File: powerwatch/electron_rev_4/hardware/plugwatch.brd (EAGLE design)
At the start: 57.1 x 93 mm, 124 parts, among them J1 DM3AT-SF-PEJM5, J2 TC2030-JLINK-NL, Q1 SI223DDS, U1 BGA725L6-ALT, U10 SIP32510, U11 SIP32510, U12 SIP32510, U13 SIP32510, U14 MPU-9250, U15 TPS3839G25DBZ, U2 SAFFB1G56KB0F0A, U3 ISL29035, U4 MAX-M8, U5 MAX740XESA, U6 SIP32510, U7 NRF51822QF, U8 OPA322AIDBVT, U9 SIP32510, X1 32.768k, X2 16MHz

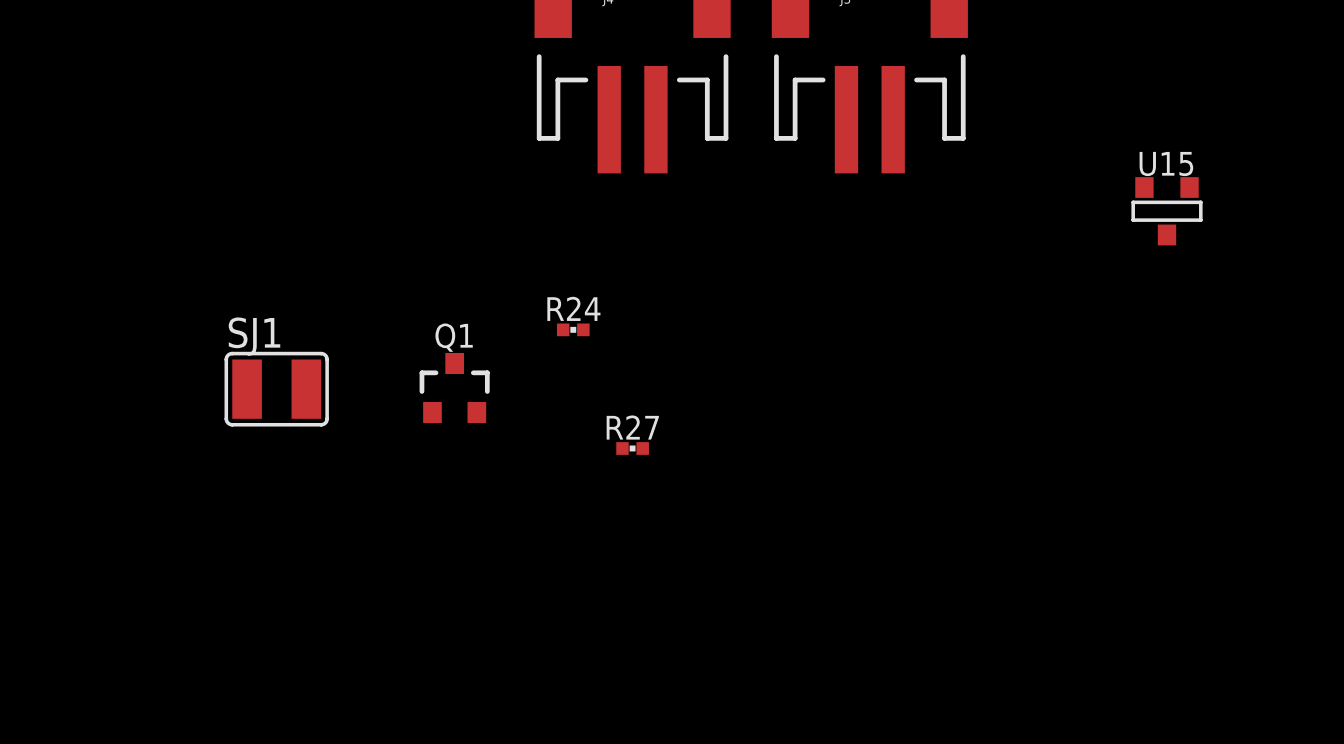
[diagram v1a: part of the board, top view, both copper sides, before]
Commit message: change voltage input to also have WDI
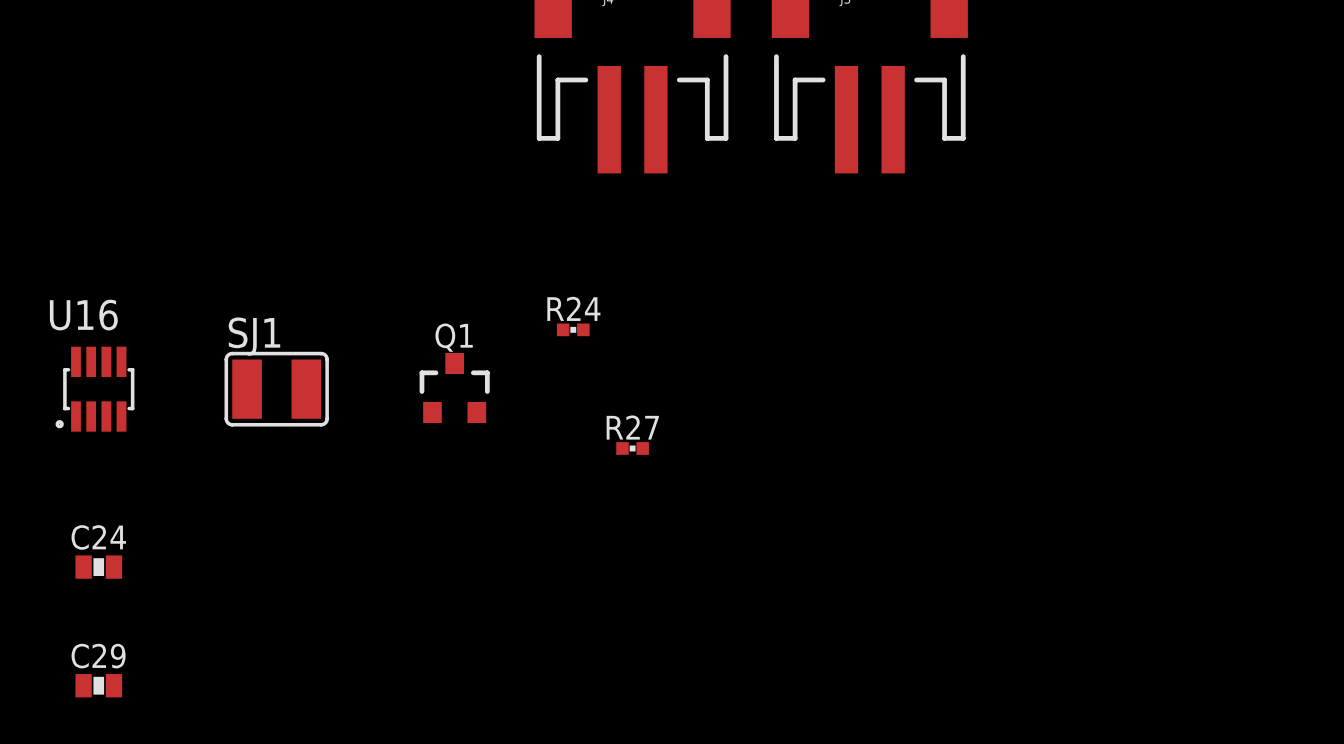
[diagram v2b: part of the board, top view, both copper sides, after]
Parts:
- removed U15: TPS3839G25DBZ, chips:SOT-23
- added C24: 0.82uF, passives:0603_CAP
- added C29: 0.47uF, passives:0603_CAP
- added U16: MAX6746, chips:SOT-23-8
- R24: value 10.4k -> 835k
- R27: value 101k -> 500k
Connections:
- removed net N$30: R24.2, R27.1, U15.3
- new net N$31: R24.2, R27.1, U16.1
- new net N$36: C24.1, U16.3
- new net N$39: C29.1, U16.2
- new net WDI: ASSY1.DAC, U16.6
- net !EXTERNAL_RST: now also U16.7; no longer U15.2
- net GND: now also C24.2, C29.2, U16.4; no longer U15.1
- net N$23: now also U16.5, U16.8
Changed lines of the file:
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@@
 <attribute name="VALUE" x="43.053" y="88.9" size="1.016" layer="28" font="vector" ratio="12" rot="MR270" align="bottom-center"/>
-</element>
-<element name="U15" library="chips" package="SOT-23" value="TPS3839G25DBZ" x="-10.16" y="0">
-<attribute name="DIGIKEY" value="296-42522-1-ND" x="-10.16" y="0" size="1.778" layer="27" font="vector" ratio="12" display="off"/>
-<attribute name="MANUFACTURER" value="TEXAS INSTRUMENTS" x="-10.16" y="0" size="1.778" layer="27" font="vector" ratio="12" display="off"/>
-<attribute name="MPN" value="TPS3839G25DBZR" x="-10.16" y="0" size="1.778" layer="27" font="vector" ratio="12" display="off"/>
 </element>
 <element name="J3" library="SparkFun-Connectors" package="JST-2-SMD" value="" x="-22.86" y="7.62">
@@
 <attribute name="PROD_ID" value="CONN-08352" x="-33.02" y="7.62" size="1.778" layer="27" font="vector" ratio="12" display="off"/>
 </element>
-<element name="R24" library="passives" package="0402_RES" value="10.4k" x="-35.56" y="-5.08">
+<element name="R24" library="passives" package="0402_RES" value="835k" x="-35.56" y="-5.08">
 <attribute name="DESCRIPTION" value="RES SMD 150 OHM 1% 1/16W 0402" x="-33.02" y="-5.08" size="1.778" layer="27" font="vector" ratio="12" display="off"/>
 <attribute name="DIGIKEY" value="RMCF0402FT150RCT-ND" x="-33.02" y="-5.08" size="1.778" layer="27" font="vector" ratio="12" display="off"/>
@@
 <attribute name="MPN" value="RMCF0402FT150R" x="-33.02" y="-5.08" size="1.778" layer="27" font="vector" ratio="12" display="off"/>
 </element>
-<element name="R27" library="passives" package="0402_RES" value="101k" x="-33.02" y="-10.16">
+<element name="R27" library="passives" package="0402_RES" value="500k" x="-33.02" y="-10.16">
 <attribute name="DESCRIPTION" value="RES SMD 150 OHM 1% 1/16W 0402" x="-33.02" y="-10.16" size="1.778" layer="27" font="vector" ratio="12" display="off"/>
 <attribute name="DIGIKEY" value="RMCF0402FT150RCT-ND" x="-33.02" y="-10.16" size="1.778" layer="27" font="vector" ratio="12" display="off"/>
@@
 </element>
 <element name="SJ1" library="jumper" library_urn="urn:adsk.eagle:library:252" package="SJW" package3d_urn="urn:adsk.eagle:package:15507/1" value="" x="-48.26" y="-7.62"/>
+<element name="U16" library="chips" package="SOT-23-8" value="MAX6746" x="-55.88" y="-7.62">
+<attribute name="DIGIKEY" value="MAX6749KA" x="-55.88" y="-7.62" size="1.778" layer="27" font="vector" ratio="12" display="off"/>
+</element>
+<element name="C24" library="passives" package="0603_CAP" value="0.82uF" x="-55.88" y="-15.24"/>
+<element name="C29" library="passives" package="0603_CAP" value="0.47uF" x="-55.88" y="-20.32"/>
 </elements>
 <signals>
@@
 <contactref element="R17" pad="1"/>
 <contactref element="J3" pad="1"/>
-<contactref element="U15" pad="1"/>
+<contactref element="J4" pad="1"/>
 <contactref element="R27" pad="2"/>
-<contactref element="J4" pad="1"/>
+<contactref element="U16" pad="4"/>
+<contactref element="C24" pad="2"/>
+<contactref element="C29" pad="2"/>
 <wire x1="50.292" y1="71.628" x2="52.832" y2="71.628" width="0" layer="19" extent="1-1"/>
 <wire x1="45.466" y1="73.152" x2="50.292" y2="71.628" width="0" layer="19" extent="1-1"/>
@@
 <wire x1="10.668" y1="35.052" x2="5.701" y2="38" width="0" layer="19" extent="1-1"/>
 <wire x1="14.65453125" y1="41.7068" x2="13.97" y2="42.418" width="0" layer="19" extent="1-1"/>
-<wire x1="-9.1694" y1="1.016" x2="1.27" y2="1.27" width="0" layer="19" extent="1-1"/>
-<wire x1="-23.86" y1="3.92" x2="-9.1694" y2="1.016" width="0" layer="19" extent="1-1"/>
-<wire x1="-34.02" y1="3.92" x2="-23.86" y2="3.92" width="0" layer="19" extent="1-1"/>
-<wire x1="-32.58693125" y1="-10.16" x2="-34.02" y2="3.92" width="0" layer="19" extent="1-1"/>
 <wire x1="32.004" y1="88.647" x2="43.942" y2="75.184" width="0" layer="19" extent="16-16"/>
 <wire x1="28.956" y1="89.916" x2="32.004" y2="88.647" width="0" layer="19" extent="16-16"/>
@@
 <wire x1="10.08506875" y1="69.342" x2="7.85" y2="68.996" width="0" layer="19" extent="16-16"/>
 <wire x1="2.794" y1="65.024" x2="5.35" y2="68.096" width="0" layer="19" extent="16-16"/>
+<wire x1="-23.86" y1="3.92" x2="1.27" y2="3.81" width="0" layer="19" extent="1-1"/>
+<wire x1="-34.02" y1="3.92" x2="-23.86" y2="3.92" width="0" layer="19" extent="1-1"/>
+<wire x1="-32.58693125" y1="-10.16" x2="-34.02" y2="3.92" width="0" layer="19" extent="1-1"/>
+<wire x1="-54.905" y1="-8.79" x2="-32.58693125" y2="-10.16" width="0" layer="19" extent="1-1"/>
+<wire x1="-55.23" y1="-15.24" x2="-54.905" y2="-8.79" width="0" layer="19" extent="1-1"/>
+<wire x1="-55.23" y1="-20.32" x2="-55.23" y2="-15.24" width="0" layer="19" extent="1-1"/>
 </signal>
 <signal name="GPS_PWR_EN">
@@
 <signal name="N$23">
 <contactref element="J3" pad="2"/>
-<contactref element="R24" pad="1"/>
 <contactref element="Q1" pad="2"/>
 <contactref element="SJ1" pad="1"/>
+<contactref element="U16" pad="8"/>
+<contactref element="R24" pad="1"/>
+<contactref element="U16" pad="5"/>
+<wire x1="-54.905" y1="-6.45" x2="-56.855" y2="-6.45" width="0" layer="19" extent="1-1"/>
+<wire x1="-49.53" y1="-7.62" x2="-54.905" y2="-6.45" width="0" layer="19" extent="1-1"/>
 <wire x1="-39.69" y1="-8.62" x2="-49.53" y2="-7.62" width="0" layer="19" extent="1-1"/>
 <wire x1="-35.99306875" y1="-5.08" x2="-39.69" y2="-8.62" width="0" layer="19" extent="1-1"/>
 <wire x1="-21.86" y1="3.92" x2="-35.99306875" y2="-5.08" width="0" layer="19" extent="1-1"/>
 </signal>
-<signal name="N$30">
-<contactref element="R24" pad="2"/>
-<contactref element="R27" pad="1"/>
-<contactref element="U15" pad="3"/>
-<wire x1="-35.12693125" y1="-5.08" x2="-33.45306875" y2="-10.16" width="0" layer="19" extent="1-1"/>
-<wire x1="-10.1346" y1="-1.016" x2="-33.45306875" y2="-10.16" width="0" layer="19" extent="1-1"/>
-</signal>
 <signal name="!EXTERNAL_RST">
-<contactref element="U15" pad="2"/>
 <contactref element="Q1" pad="1"/>
 <contactref element="ASSY1" pad="RST"/>
-<wire x1="-11.0998" y1="1.016" x2="24.0538" y2="45.6692" width="0" layer="19" extent="1-1"/>
-<wire x1="-41.59" y1="-8.62" x2="-11.0998" y2="1.016" width="0" layer="19" extent="1-1"/>
+<contactref element="U16" pad="7"/>
+<wire x1="-41.59" y1="-8.62" x2="24.0538" y2="45.6692" width="0" layer="19" extent="1-1"/>
+<wire x1="-56.205" y1="-6.45" x2="-41.59" y2="-8.62" width="0" layer="19" extent="1-1"/>
 </signal>
 <signal name="N$35">
@@
 <wire x1="48.095" y1="10.45" x2="41.8338" y2="71.0692" width="0" layer="19" extent="16-16"/>
 </signal>
+<signal name="N$31">
+<contactref element="R24" pad="2"/>
+<contactref element="R27" pad="1"/>
+<contactref element="U16" pad="1"/>
+<wire x1="-35.12693125" y1="-5.08" x2="-56.855" y2="-8.79" width="0" layer="19" extent="1-1"/>
+<wire x1="-33.45306875" y1="-10.16" x2="-35.12693125" y2="-5.08" width="0" layer="19" extent="1-1"/>
+</signal>
+<signal name="N$36">
+<contactref element="U16" pad="3"/>
+<contactref element="C24" pad="1"/>
+<wire x1="-55.555" y1="-8.79" x2="-56.53" y2="-15.24" width="0" layer="19" extent="1-1"/>
+</signal>
+<signal name="N$39">
+<contactref element="C29" pad="1"/>
+<contactref element="U16" pad="2"/>
+<wire x1="-56.205" y1="-8.79" x2="-56.53" y2="-20.32" width="0" layer="19" extent="1-1"/>
+</signal>
+<signal name="WDI">
+<contactref element="U16" pad="6"/>
+<contactref element="ASSY1" pad="DAC"/>
+<wire x1="-55.555" y1="-6.45" x2="41.8338" y2="55.8292" width="0" layer="19" extent="1-1"/>
+</signal>
 </signals>

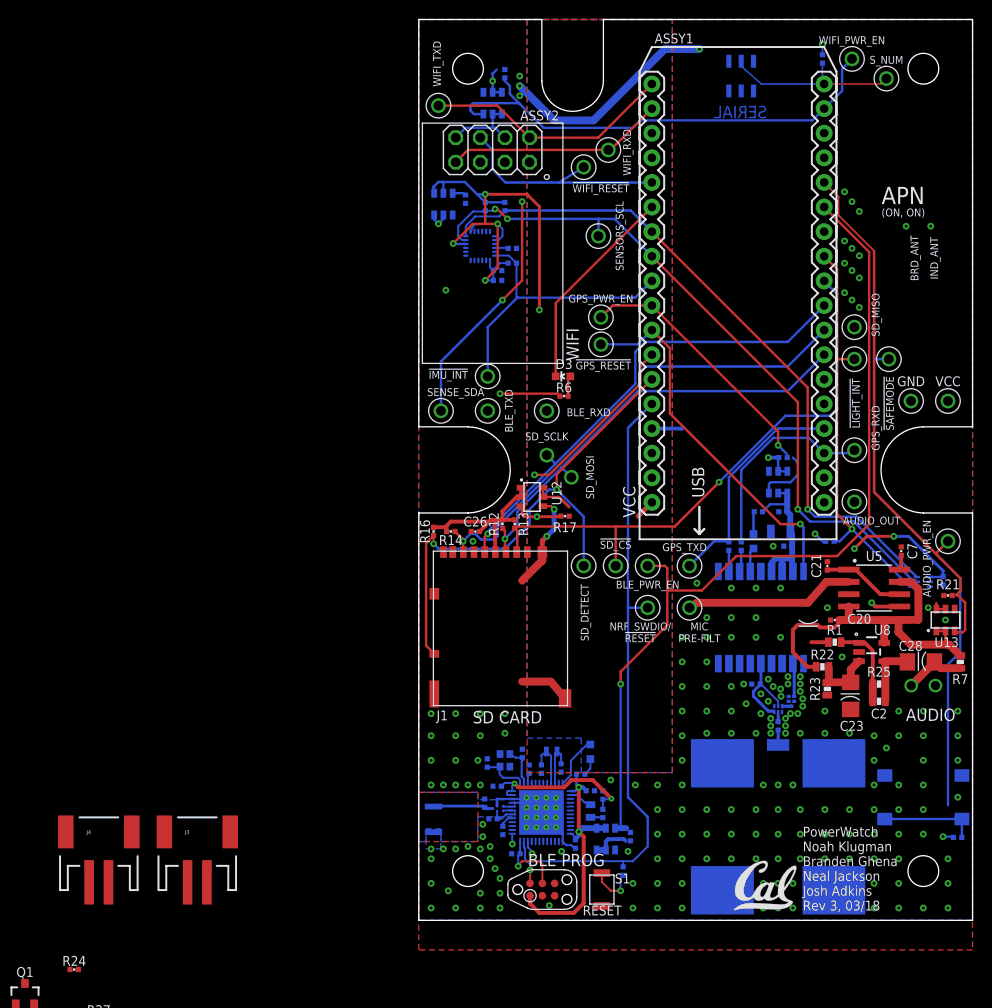
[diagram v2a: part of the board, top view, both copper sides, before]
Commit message: add new power supply with updated board shape
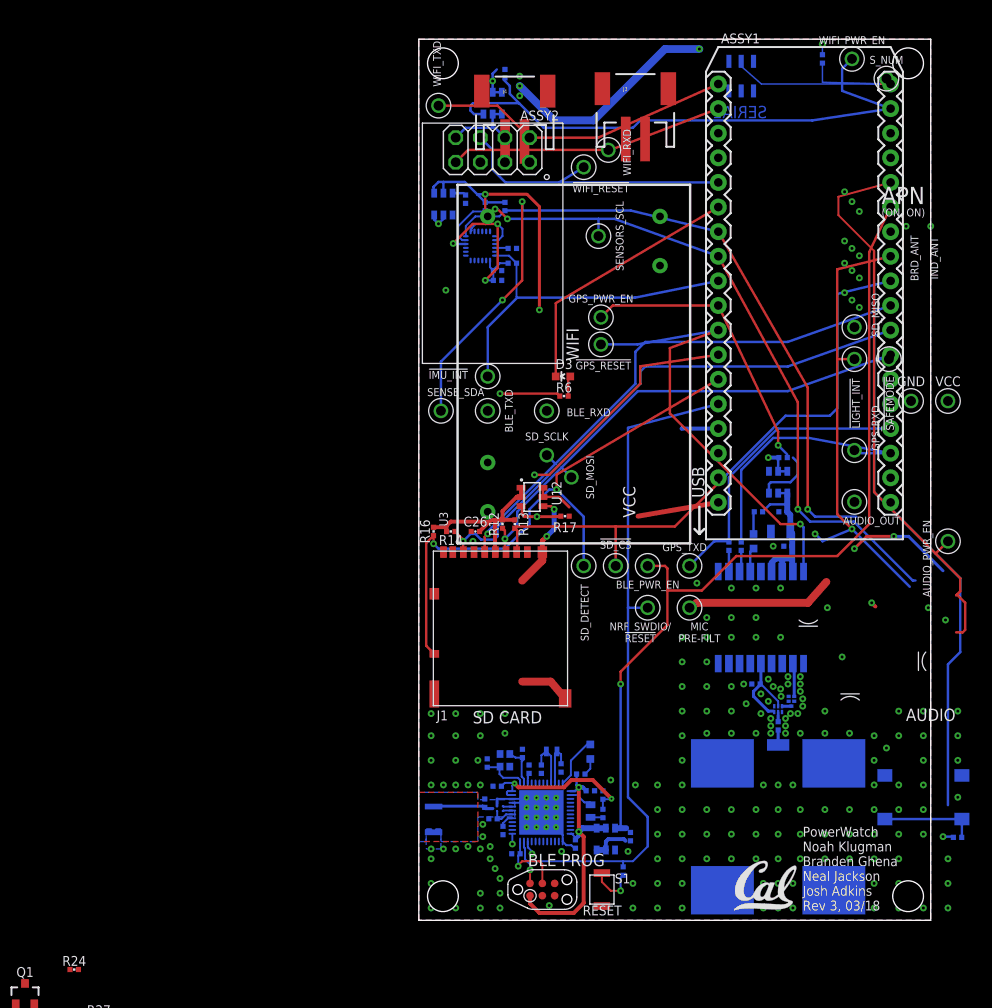
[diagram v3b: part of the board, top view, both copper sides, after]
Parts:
- removed C17, C20, C21: 100nF, passives:0402_CAP
- removed C2: 4.4pF, passives:0603_CAP
- removed C23: 2.2uF, passives:1206
- removed C28: 10uF, passives:1206
- removed C7: 330pF, passives:0402_CAP
- removed MK1: AOM-4546P-R, microphones:MIC_AOM-4546P-R
- removed R1: 49.9, passives:0603-RES
- removed R21: 100k, passives:0402_RES
- removed R22, R23: 100k, passives:0603-RES
- removed R25: 270k, passives:0603-RES
- removed R7: 3.48k, passives:0603-RES
- removed R8: 10k, passives:0402_RES
- removed U13: SIP32510, chips:TSOT23-6
- removed U5: MAX740XESA, chips:SOIC-8
- removed U8: OPA322AIDBVT, opamps:SOT23-5
- U3: value ISL29035 -> IRM-03-5V; device chips:ODFN-6-1.5MMX1.6MM -> powerwatch:IRM-03
- moved J3 89.0 mm to (22.4, 84.3)
- moved J4 87.7 mm to (9.91, 84.1)
- moved U3 42.5 mm to (16.0, 57.4), flipped to the top, turned to 90 degrees
- moved ASSY1 6.86 mm to (50.0, 39.3)
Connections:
- removed net -AMP: C2.1, C28.2, R25.2, U8.4
- removed net N$11: C21.1, U5.1, U5.6
- removed net N$4: C28.1, MK1.TERM+, R7.1
- removed net N$5: C2.2, R1.2, R25.1, U8.1
- removed net N$6: C7.2, U5.8
- removed net N$7: R1.1
- removed net N$9: C23.2, R22.1, R23.2, U8.3
- removed net VCC_A_MIC: C20.1, R22.2, R7.2, U13.1, U13.2, U5.4, U5.7, U8.5
- new net N$30: R26.1, U6.4
- net !LIGHT_INT: no longer R8.1, U3.4
- net AUDIO_OUT: no longer U5.5
- net AUDIO_PWR_EN: no longer R21.2, U13.3
- net A_MIC_OUT: no longer U5.2
- net GND: no longer C17.2, C20.2, C21.2, C23.1, C7.1, MK1.TERM-, R21.1, R23.1, R26.1, U13.4, U3.2, U5.3, U6.4, U8.2
- net SENSORS_SCL: no longer U3.5
- net SENSORS_SDA: no longer U3.6
- net VCC: no longer U13.5, U13.6
- net VCC_SENSORS: no longer C17.1, R8.2, U3.1
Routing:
- net VCC_A_MIC: track 39.5 -> 0.00 mm
- net SD_MISO: track 53.9 -> 65.9 mm
- net WIFI_PWR_EN: track 50.3 -> 59.5 mm
- net !GPS_RESET: track 38.5 -> 47.5 mm
- net N$5: track 8.86 -> 0.00 mm
- net SERIAL_NUM: track 18.6 -> 27.4 mm
- net N$11: track 8.52 -> 0.00 mm
- net GPS_RXD: track 21.3 -> 28.8 mm
- net GPS_TXD: track 23.7 -> 30.6 mm
- net !WIFI_RESET: track 23.8 -> 30.7 mm
- net SENSORS_SDA: track 97.3 -> 90.5 mm
- net N$9: track 6.65 -> 0.00 mm
- net -AMP: track 6.58 -> 0.00 mm
- net SD_ENABLE: track 27.6 -> 34.0 mm
- net N$4: track 6.37 -> 0.00 mm
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- removed copper zone on layer 1, net N$33
- removed copper zone on layer 16, net N$33
- removed copper zone on layer 2, net N$33
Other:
- board size 57.1 x 93 mm -> 52.8 x 90.9 mm

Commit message: added AC voltage sense and perturb/observe cap sensing
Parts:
- added AC/L, AC/N: TEST_POINT_0.060IN, headers:TESTPOINT_0.060IN
- added C100, C101: 0.1uF, passives:0603_CAP
- added C17, C7: 100uF, passives:1210_CAP
- added C2: 2000uF, rcl:E5-13
- added D10, D11, D8, D9: (no value), passives:SOD323
- added D4, D5, D6, D7: 3.3V, passives:SOD323
- added F1: 300VAC - 500ma, powerwatch:MIRCRO_FUSE_5MM
- added Q2: MOSFET-NCHANNELSMD, fets:SOT23-3
- added R1: 100, passives:0402_RES
- added R21, R30, R31, R8: 750k, passives:0402_RES
- added R22, R25: 1M 1%, rcl:R0402
- added R23, R28: 1M 1%, rcl:R0402_SM
- added R7: S14K385, varistor:S14K385
- added RF, RF1: 4.99k 1%, rcl:R0402
- added RI1, RI2, RI3, RI4: 953k 1%, rcl:R0402
- added U5, U8: MAX9910, powerfilm:SC70-5
- moved U3 72.0 mm to (84.8, 36.3), turned to 180 degrees
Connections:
- removed net VIN: ASSY1.VIN
- new net 5V: ASSY1.VIN, C17.1, C2.+, C7.1, R1.1, U3.V+
- new net AC/L-FUSED: F1.P$2, R30.1, R7.1, R8.1, RI1.1, U3.AC/L
- new net AC/L-MEASURE: D6.P$1, D8.P$1, R30.2
- new net AC/L-PERTURB: D4.P$1, D9.P$1, R8.2
- new net AC/L-SENSE: RF.2, U5.P4
- new net AC/N-FUSED: AC/N.TESTPOINT, R21.1, R31.1, R7.2, RI3.1, U3.AC/N
- new net AC/N-MEASURE: D10.P$1, D5.P$1, R31.2
- new net AC/N-PERTURB: D11.P$1, D7.P$1, R21.2
- new net AC/N-SENSE: RF1.2, U8.P4
- new net N$32: Q2.1, R1.2
- new net N$38: AC/L.TESTPOINT, F1.P$1
- new net N$42: R22.1, R23.2, U5.P1
- new net N$43: RF.1, RI1.2, RI2.2, U5.P3
- new net N$44: R25.1, R28.2, U8.P1
- new net N$45: RF1.1, RI3.2, RI4.2, U8.P3
- new net N$9: C17.2, C2.-, C7.2, Q2.3, U3.V-
- net GND: now also C100.2, C101.2, D10.P$2, D11.P$2, D4.P$2, D5.P$2, D6.P$2, D7.P$2, D8.P$2, D9.P$2, Q2.2, R23.1, R28.1, RI2.1, RI4.1, U5.P2, U8.P2
- net VCC: now also C100.1, C101.1, R22.2, R25.2, U5.P5, U8.P5
